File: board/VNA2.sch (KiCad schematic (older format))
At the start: 78 parts, among them U2 74HC14, U3 SA612, U4 SA612, U5 SA612, U6 TL082, U7 TL082, U8 SA612

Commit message: Removed useless parts of the board and make some corrections
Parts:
- removed C37, C38, C41, C42: 10 nF, Capacitors_THT:C_Disc_D5.0mm_W2.5mm_P2.50mm, symbol C_Small
- removed C39: 330 pF, Capacitors_THT:C_Disc_D5.0mm_W2.5mm_P2.50mm, symbol C_Small
- removed C43, C45: 100 nF, Capacitors_THT:C_Disc_D5.0mm_W2.5mm_P2.50mm, symbol C_Small
- removed C44: 1 nF, Capacitors_THT:C_Disc_D5.0mm_W2.5mm_P2.50mm, symbol C_Small
- removed JP3: Jumper_NC_Dual, Pin_Headers:Pin_Header_Straight_1x03_Pitch2.54mm, symbol Jumper_NC_Dual
- removed L6: Ferrite_Bead_Small, Inductors_THT:L_Axial_L5.3mm_D2.2mm_P7.62mm_Horizontal_Vishay_IM-1, symbol Ferrite_Bead_Small
- removed R34: 51R, Resistors_THT:R_Axial_DIN0207_L6.3mm_D2.5mm_P7.62mm_Horizontal, symbol R
- removed R35: 1.5k, Resistors_THT:R_Axial_DIN0207_L6.3mm_D2.5mm_P7.62mm_Horizontal, symbol R
- removed R36, R37, R38: 2.2k, Resistors_THT:R_Axial_DIN0207_L6.3mm_D2.5mm_P7.62mm_Horizontal, symbol R
- removed RV1, RV2, RV3: 22k, Potentiometers:Potentiometer_Trimmer_Bourns_3296W, symbol POT
- removed U8: SA612, Housings_DIP:DIP-8_W7.62mm_Socket, symbol SA612
- added unit 1 of U2
- added unit 2 of U2
- C10, C11, C12, C13, C20, C21, C24, C8, C9: value 10 nF -> 100 nF
- R19, R20, R21, R25, R26, R27: value 10k -> 1k5
- R22, R23, R24: value 47k -> 68k
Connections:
- net labels removed: CLK0, CLK2, SYNCSAMPLEP1, SYNCSAMPLEP2, SYNCSAMPLEP3
- wire segments 229 -> 172
- no-connect marks 8 -> 11

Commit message: Added LCD mount
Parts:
- removed C40: 100 nF, Capacitors_THT:C_Disc_D5.0mm_W2.5mm_P2.50mm, symbol C_Small
- removed D5, D6: 1N4148, Diodes_THT:D_DO-35_SOD27_P7.62mm_Horizontal, symbol D
- removed R39: 1k, Resistors_THT:R_Axial_DIN0207_L6.3mm_D2.5mm_P7.62mm_Horizontal, symbol R
- removed R40, R41: 10k, Resistors_THT:R_Axial_DIN0207_L6.3mm_D2.5mm_P7.62mm_Horizontal, symbol R
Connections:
- net labels added: SYNCSAMPLE2
- wire segments 172 -> 157
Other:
- moved on the sheet: U7B

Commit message: Substitute LM339 for 74HC14
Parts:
- removed U2: 74HC14, Housings_DIP:DIP-14_W7.62mm_Socket, symbol 74HC14
- added C37: 100 nF, Capacitors_THT:C_Disc_D5.0mm_W2.5mm_P2.50mm, symbol C_Small
- added R10, R7: 10k, Resistors_THT:R_Axial_DIN0207_L6.3mm_D2.5mm_P7.62mm_Horizontal, symbol R
- added R34, R35: 1M, Resistors_THT:R_Axial_DIN0207_L6.3mm_D2.5mm_P7.62mm_Horizontal, symbol R
- added R36, R37: 1k, Resistors_THT:R_Axial_DIN0207_L6.3mm_D2.5mm_P7.62mm_Horizontal, symbol R
- added U2: LM339, Housings_DIP:DIP-14_W7.62mm_Socket, symbol LM339
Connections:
- wire segments 157 -> 176
- no-connect marks 11 -> 6
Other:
- moved on the sheet: U7B

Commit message: JLCPCB order 2018-12-01
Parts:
- added R41: 1k, Resistors_THT:R_Axial_DIN0207_L6.3mm_D2.5mm_P7.62mm_Horizontal, symbol R
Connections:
- net at C29.1, R22.2, R32.2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: now also R41.2; no longer U2.6 (-)
- new net: R41.1, U2.6 (-)
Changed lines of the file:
@@
 $EndComp
 $Comp
-L GND #PWR46
+L GND #PWR49
 U 1 1 5BB32DBE
 P 3150 950
-F 0 "#PWR46" H 3150 700 50  0001 C CNN
+F 0 "#PWR49" H 3150 700 50  0001 C CNN
 F 1 "GND" H 3150 800 50  0000 C CNN
 F 2 "" H 3150 950 50  0001 C CNN
@@
 $EndComp
 $Comp
-L GND #PWR37
+L GND #PWR40
 U 1 1 5BB32DD3
 P 1100 1700
-F 0 "#PWR37" H 1100 1450 50  0001 C CNN
+F 0 "#PWR40" H 1100 1450 50  0001 C CNN
 F 1 "GND" H 1100 1550 50  0000 C CNN
 F 2 "" H 1100 1700 50  0001 C CNN
@@
 $EndComp
 $Comp
-L GND #PWR40
+L GND #PWR43
 U 1 1 5BB32DD9
 P 1500 1800
-F 0 "#PWR40" H 1500 1550 50  0001 C CNN
+F 0 "#PWR43" H 1500 1550 50  0001 C CNN
 F 1 "GND" H 1500 1650 50  0000 C CNN
 F 2 "" H 1500 1800 50  0001 C CNN
@@
 $EndComp
 $Comp
-L GND #PWR43
+L GND #PWR46
 U 1 1 5BB32DF0
 P 1900 2250
-F 0 "#PWR43" H 1900 2000 50  0001 C CNN
+F 0 "#PWR46" H 1900 2000 50  0001 C CNN
 F 1 "GND" H 1900 2100 50  0000 C CNN
 F 2 "" H 1900 2250 50  0001 C CNN
@@
 $EndComp
 $Comp
-L GND #PWR48
+L GND #PWR51
 U 1 1 5BB32E0B
 P 4350 2450
-F 0 "#PWR48" H 4350 2200 50  0001 C CNN
+F 0 "#PWR51" H 4350 2200 50  0001 C CNN
 F 1 "GND" H 4350 2300 50  0000 C CNN
 F 2 "" H 4350 2450 50  0001 C CNN
@@
 FILT5V
 $Comp
-L GND #PWR50
+L GND #PWR53
 U 1 1 5BB32E19
 P 4650 1800
-F 0 "#PWR50" H 4650 1550 50  0001 C CNN
+F 0 "#PWR53" H 4650 1550 50  0001 C CNN
 F 1 "GND" H 4650 1650 50  0000 C CNN
 F 2 "" H 4650 1800 50  0001 C CNN
@@
 $EndComp
 $Comp
-L GND #PWR45
+L GND #PWR48
 U 1 1 5BB32E52
 P 3100 2750
-F 0 "#PWR45" H 3100 2500 50  0001 C CNN
+F 0 "#PWR48" H 3100 2500 50  0001 C CNN
 F 1 "GND" H 3100 2600 50  0000 C CNN
 F 2 "" H 3100 2750 50  0001 C CNN
@@
 $EndComp
 $Comp
-L GND #PWR36
+L GND #PWR39
 U 1 1 5BB32E67
 P 1050 3500
-F 0 "#PWR36" H 1050 3250 50  0001 C CNN
+F 0 "#PWR39" H 1050 3250 50  0001 C CNN
 F 1 "GND" H 1050 3350 50  0000 C CNN
 F 2 "" H 1050 3500 50  0001 C CNN
@@
 $EndComp
 $Comp
-L GND #PWR39
+L GND #PWR42
 U 1 1 5BB32E6D
 P 1450 3600
-F 0 "#PWR39" H 1450 3350 50  0001 C CNN
+F 0 "#PWR42" H 1450 3350 50  0001 C CNN
 F 1 "GND" H 1450 3450 50  0000 C CNN
 F 2 "" H 1450 3600 50  0001 C CNN
@@
 $EndComp
 $Comp
-L GND #PWR42
+L GND #PWR45
 U 1 1 5BB32E84
 P 1850 4050
-F 0 "#PWR42" H 1850 3800 50  0001 C CNN
+F 0 "#PWR45" H 1850 3800 50  0001 C CNN
 F 1 "GND" H 1850 3900 50  0000 C CNN
 F 2 "" H 1850 4050 50  0001 C CNN
@@
 $EndComp
 $Comp
-L GND #PWR52
+L GND #PWR55
 U 1 1 5BB32ED8
 P 5700 2600
-F 0 "#PWR52" H 5700 2350 50  0001 C CNN
+F 0 "#PWR55" H 5700 2350 50  0001 C CNN
 F 1 "GND" H 5700 2450 50  0000 C CNN
 F 2 "" H 5700 2600 50  0001 C CNN
@@
 $EndComp
 $Comp
-L GND #PWR54
+L GND #PWR57
 U 1 1 5BB32EE5
 P 6000 2600
-F 0 "#PWR54" H 6000 2350 50  0001 C CNN
+F 0 "#PWR57" H 6000 2350 50  0001 C CNN
 F 1 "GND" H 6000 2450 50  0000 C CNN
 F 2 "" H 6000 2600 50  0001 C CNN
@@
 $EndComp
 $Comp
-L GND #PWR56
+L GND #PWR59
 U 1 1 5BB32EFA
 P 6200 3650
-F 0 "#PWR56" H 6200 3400 50  0001 C CNN
+F 0 "#PWR59" H 6200 3400 50  0001 C CNN
 F 1 "GND" H 6200 3500 50  0000 C CNN
 F 2 "" H 6200 3650 50  0001 C CNN
@@
 $EndComp
 $Comp
-L GND #PWR57
+L GND #PWR60
 U 1 1 5BB32F07
 P 6500 3650
-F 0 "#PWR57" H 6500 3400 50  0001 C CNN
+F 0 "#PWR60" H 6500 3400 50  0001 C CNN
 F 1 "GND" H 6500 3500 50  0000 C CNN
 F 2 "" H 6500 3650 50  0001 C CNN
@@
 $EndComp
 $Comp
-L GND #PWR47
+L GND #PWR50
 U 1 1 5BB496C5
 P 3300 4800
-F 0 "#PWR47" H 3300 4550 50  0001 C CNN
+F 0 "#PWR50" H 3300 4550 50  0001 C CNN
 F 1 "GND" H 3300 4650 50  0000 C CNN
 F 2 "" H 3300 4800 50  0001 C CNN
@@
 $EndComp
 $Comp
-L GND #PWR38
+L GND #PWR41
 U 1 1 5BB496D8
 P 1250 5550
-F 0 "#PWR38" H 1250 5300 50  0001 C CNN
+F 0 "#PWR41" H 1250 5300 50  0001 C CNN
 F 1 "GND" H 1250 5400 50  0000 C CNN
 F 2 "" H 1250 5550 50  0001 C CNN
@@
 $EndComp
 $Comp
-L GND #PWR41
+L GND #PWR44
 U 1 1 5BB496DE
 P 1650 5650
-F 0 "#PWR41" H 1650 5400 50  0001 C CNN
+F 0 "#PWR44" H 1650 5400 50  0001 C CNN
 F 1 "GND" H 1650 5500 50  0000 C CNN
 F 2 "" H 1650 5650 50  0001 C CNN
@@
 $EndComp
 $Comp
-L GND #PWR44
+L GND #PWR47
 U 1 1 5BB496F3
 P 2050 6100
-F 0 "#PWR44" H 2050 5850 50  0001 C CNN
+F 0 "#PWR47" H 2050 5850 50  0001 C CNN
 F 1 "GND" H 2050 5950 50  0000 C CNN
 F 2 "" H 2050 6100 50  0001 C CNN
@@
 $EndComp
 $Comp
-L GND #PWR49
+L GND #PWR52
 U 1 1 5BB4970B
 P 4500 6300
-F 0 "#PWR49" H 4500 6050 50  0001 C CNN
+F 0 "#PWR52" H 4500 6050 50  0001 C CNN
 F 1 "GND" H 4500 6150 50  0000 C CNN
 F 2 "" H 4500 6300 50  0001 C CNN
@@
 FILT5V
 $Comp
-L GND #PWR51
+L GND #PWR54
 U 1 1 5BB49718
 P 4800 5650
-F 0 "#PWR51" H 4800 5400 50  0001 C CNN
+F 0 "#PWR54" H 4800 5400 50  0001 C CNN
 F 1 "GND" H 4800 5500 50  0000 C CNN
 F 2 "" H 4800 5650 50  0001 C CNN
@@
 $EndComp
 $Comp
-L GND #PWR53
+L GND #PWR56
 U 1 1 5BB4974C
 P 5850 6450
-F 0 "#PWR53" H 5850 6200 50  0001 C CNN
+F 0 "#PWR56" H 5850 6200 50  0001 C CNN
 F 1 "GND" H 5850 6300 50  0000 C CNN
 F 2 "" H 5850 6450 50  0001 C CNN
@@
 $EndComp
 $Comp
-L GND #PWR55
+L GND #PWR58
 U 1 1 5BB49758
 P 6150 6450
-F 0 "#PWR55" H 6150 6200 50  0001 C CNN
+F 0 "#PWR58" H 6150 6200 50  0001 C CNN
 F 1 "GND" H 6150 6300 50  0000 C CNN
 F 2 "" H 6150 6450 50  0001 C CNN
@@
 $EndComp
 $Comp
-L GND #PWR58
+L GND #PWR61
 U 1 1 5BB4F877
 P 6700 1650
-F 0 "#PWR58" H 6700 1400 50  0001 C CNN
+F 0 "#PWR61" H 6700 1400 50  0001 C CNN
 F 1 "GND" H 6700 1500 50  0000 C CNN
 F 2 "" H 6700 1650 50  0001 C CNN
@@
 	5450 3100 5450 4050
 Connection ~ 5450 3100
-Wire Wire Line
-	5450 4050 7000 4050
 Text GLabel 7950 4900 2    60   Input ~ 0
 SYNCSAMPLE2
@@
 Connection ~ 8850 1100
 $Comp
-L GND #PWR60
+L GND #PWR63
 U 1 1 5BF2333C
 P 8550 850
-F 0 "#PWR60" H 8550 600 50  0001 C CNN
+F 0 "#PWR63" H 8550 600 50  0001 C CNN
 F 1 "GND" H 8550 700 50  0000 C CNN
 F 2 "" H 8550 850 50  0001 C CNN
@@
 	8550 850  8800 850
 $Comp
-L GND #PWR62
+L GND #PWR65
 U 1 1 5BF23614
 P 8850 2000
-F 0 "#PWR62" H 8850 1750 50  0001 C CNN
+F 0 "#PWR65" H 8850 1750 50  0001 C CNN
 F 1 "GND" H 8850 1850 50  0000 C CNN
 F 2 "" H 8850 2000 50  0001 C CNN
@@
 	8850 1900 8850 2000
 $Comp
-L GND #PWR61
+L GND #PWR64
 U 1 1 5BF238FB
 P 8550 1900
-F 0 "#PWR61" H 8550 1650 50  0001 C CNN
+F 0 "#PWR64" H 8550 1650 50  0001 C CNN
 F 1 "GND" H 8550 1750 50  0000 C CNN
 F 2 "" H 8550 1900 50  0001 C CNN
@@
 	8450 2500 8650 2500
 $Comp
-L GND #PWR59
+L GND #PWR62
 U 1 1 5BF23F5D
 P 8500 2800
-F 0 "#PWR59" H 8500 2550 50  0001 C CNN
+F 0 "#PWR62" H 8500 2550 50  0001 C CNN
 F 1 "GND" H 8500 2650 50  0000 C CNN
 F 2 "" H 8500 2800 50  0001 C CNN
@@
 Wire Wire Line
 	8500 2700 8650 2700
+$Comp
+L R R41
+U 1 1 5C00ADBE
+P 6050 4050
+F 0 "R41" V 6130 4050 50  0000 C CNN
+F 1 "1k" V 6050 4050 50  0000 C CNN
+F 2 "Resistors_THT:R_Axial_DIN0207_L6.3mm_D2.5mm_P7.62mm_Horizontal" V 5980 4050 50  0001 C CNN
+F 3 "" H 6050 4050 50  0001 C CNN
+	1    6050 4050
+	0    1    1    0
+$EndComp
+Wire Wire Line
+	6200 4050 7000 4050
+Wire Wire Line
+	5450 4050 5900 4050
 $EndSCHEMATC

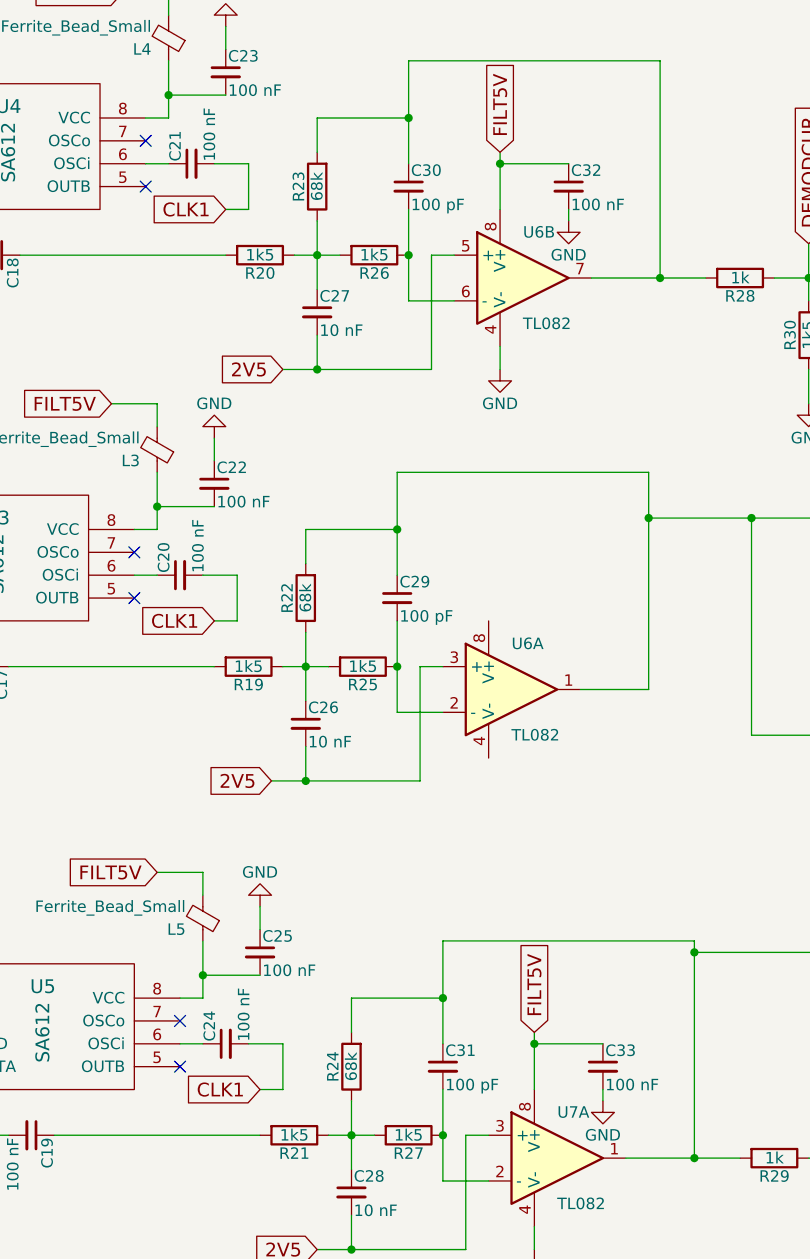
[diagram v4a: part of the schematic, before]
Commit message: Load and Save on Flash
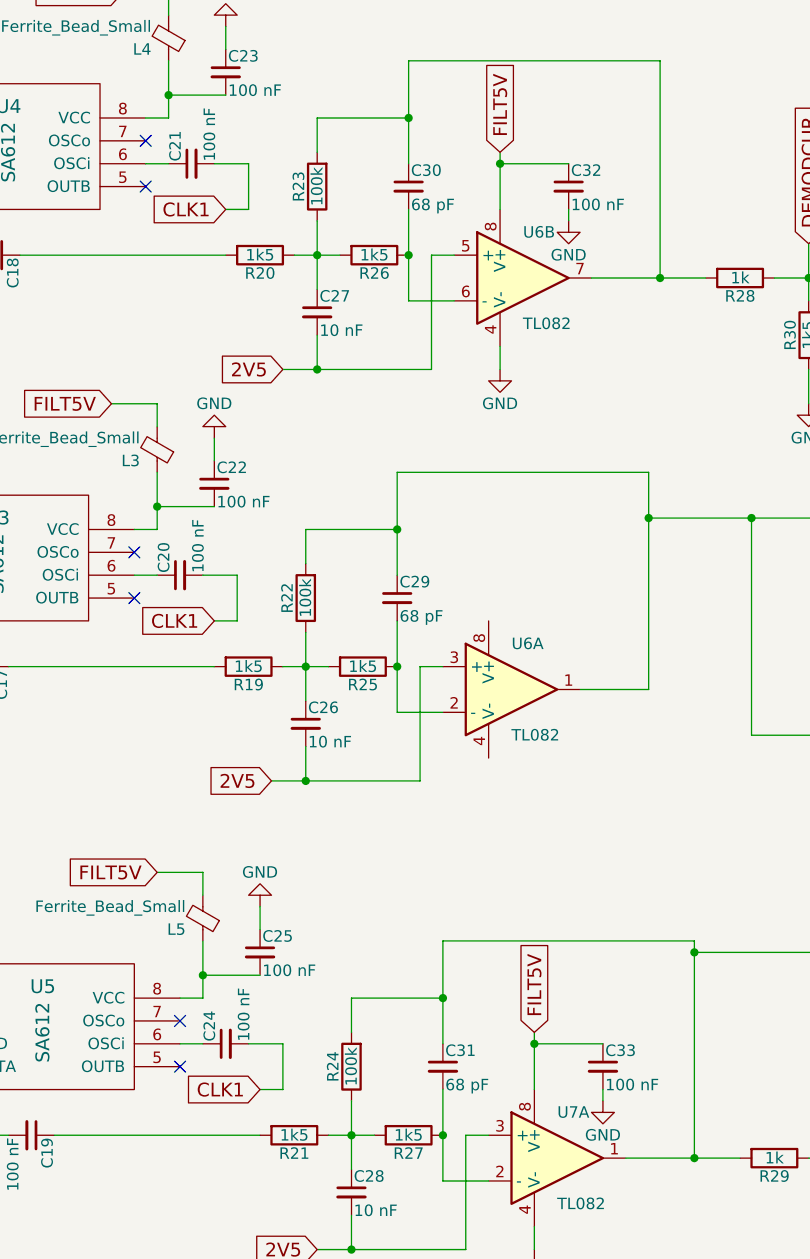
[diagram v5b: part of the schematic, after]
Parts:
- C29, C30, C31: value 100 pF -> 68 pF
- R22, R23, R24: value 68k -> 100k
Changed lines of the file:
@@
 P 3550 1650
 F 0 "R23" V 3630 1650 50  0000 C CNN
-F 1 "68k" V 3550 1650 50  0000 C CNN
+F 1 "100k" V 3550 1650 50  0000 C CNN
 F 2 "Resistors_THT:R_Axial_DIN0207_L6.3mm_D2.5mm_P7.62mm_Horizontal" V 3480 1650 50  0001 C CNN
 F 3 "" H 3550 1650 50  0001 C CNN
@@
 P 3950 1650
 F 0 "C30" H 3960 1720 50  0000 L CNN
-F 1 "100 pF" H 3960 1570 50  0000 L CNN
+F 1 "68 pF" H 3960 1570 50  0000 L CNN
 F 2 "Capacitors_THT:C_Disc_D5.0mm_W2.5mm_P2.50mm" H 3950 1650 50  0001 C CNN
 F 3 "" H 3950 1650 50  0001 C CNN
@@
 P 3500 3450
 F 0 "R22" V 3580 3450 50  0000 C CNN
-F 1 "68k" V 3500 3450 50  0000 C CNN
+F 1 "100k" V 3500 3450 50  0000 C CNN
 F 2 "Resistors_THT:R_Axial_DIN0207_L6.3mm_D2.5mm_P7.62mm_Horizontal" V 3430 3450 50  0001 C CNN
 F 3 "" H 3500 3450 50  0001 C CNN
@@
 P 3900 3450
 F 0 "C29" H 3910 3520 50  0000 L CNN
-F 1 "100 pF" H 3910 3370 50  0000 L CNN
+F 1 "68 pF" H 3910 3370 50  0000 L CNN
 F 2 "Capacitors_THT:C_Disc_D5.0mm_W2.5mm_P2.50mm" H 3900 3450 50  0001 C CNN
 F 3 "" H 3900 3450 50  0001 C CNN
@@
 P 3700 5500
 F 0 "R24" V 3780 5500 50  0000 C CNN
-F 1 "68k" V 3700 5500 50  0000 C CNN
+F 1 "100k" V 3700 5500 50  0000 C CNN
 F 2 "Resistors_THT:R_Axial_DIN0207_L6.3mm_D2.5mm_P7.62mm_Horizontal" V 3630 5500 50  0001 C CNN
 F 3 "" H 3700 5500 50  0001 C CNN
@@
 P 4100 5500
 F 0 "C31" H 4110 5570 50  0000 L CNN
-F 1 "100 pF" H 4110 5420 50  0000 L CNN
+F 1 "68 pF" H 4110 5420 50  0000 L CNN
 F 2 "Capacitors_THT:C_Disc_D5.0mm_W2.5mm_P2.50mm" H 4100 5500 50  0001 C CNN
 F 3 "" H 4100 5500 50  0001 C CNN
